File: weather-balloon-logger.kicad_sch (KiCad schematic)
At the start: 23 parts, among them J1 Conn_01x02, J2 Conn_01x11, J3 SMA, J4 SMA, J5 Conn_01x02, J6 VHF, J7 HF, Q1 IRLZ44NPBF, SW1 SPDT, U1 PCF8574N, U2 TC4422AVPA

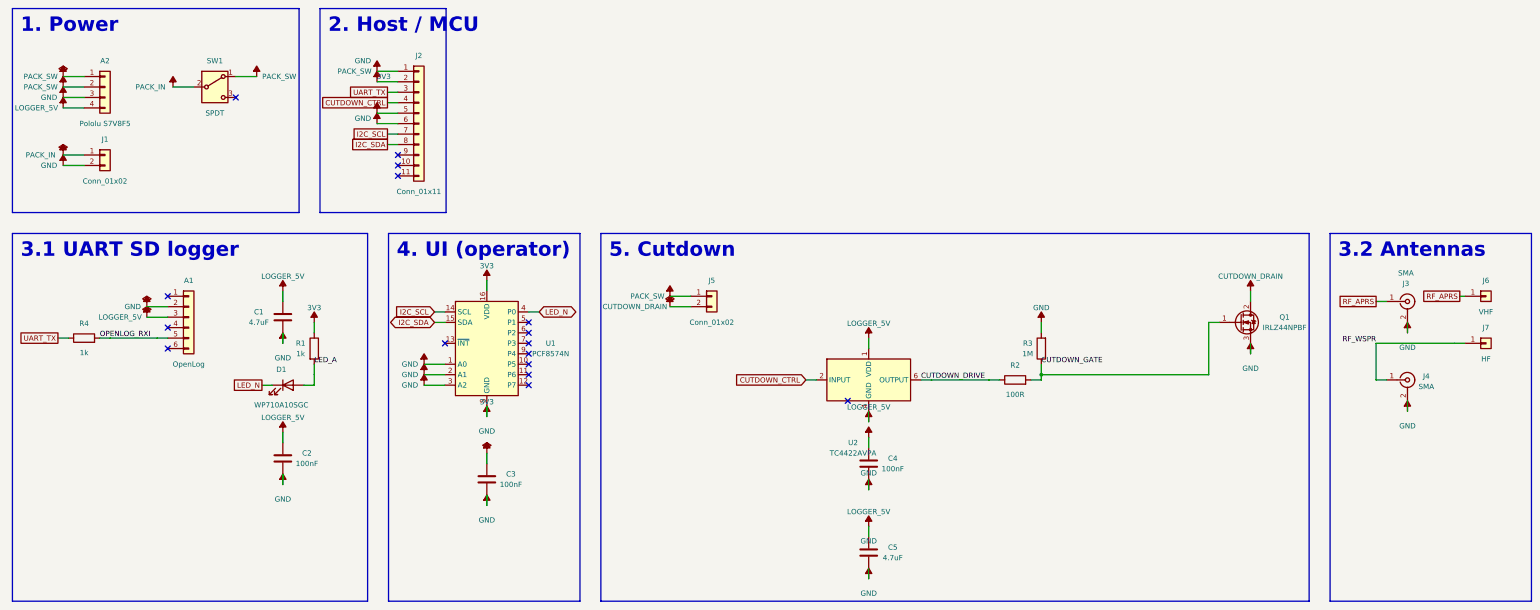
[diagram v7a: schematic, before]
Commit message: feat(schematic): migrate to LightHAB
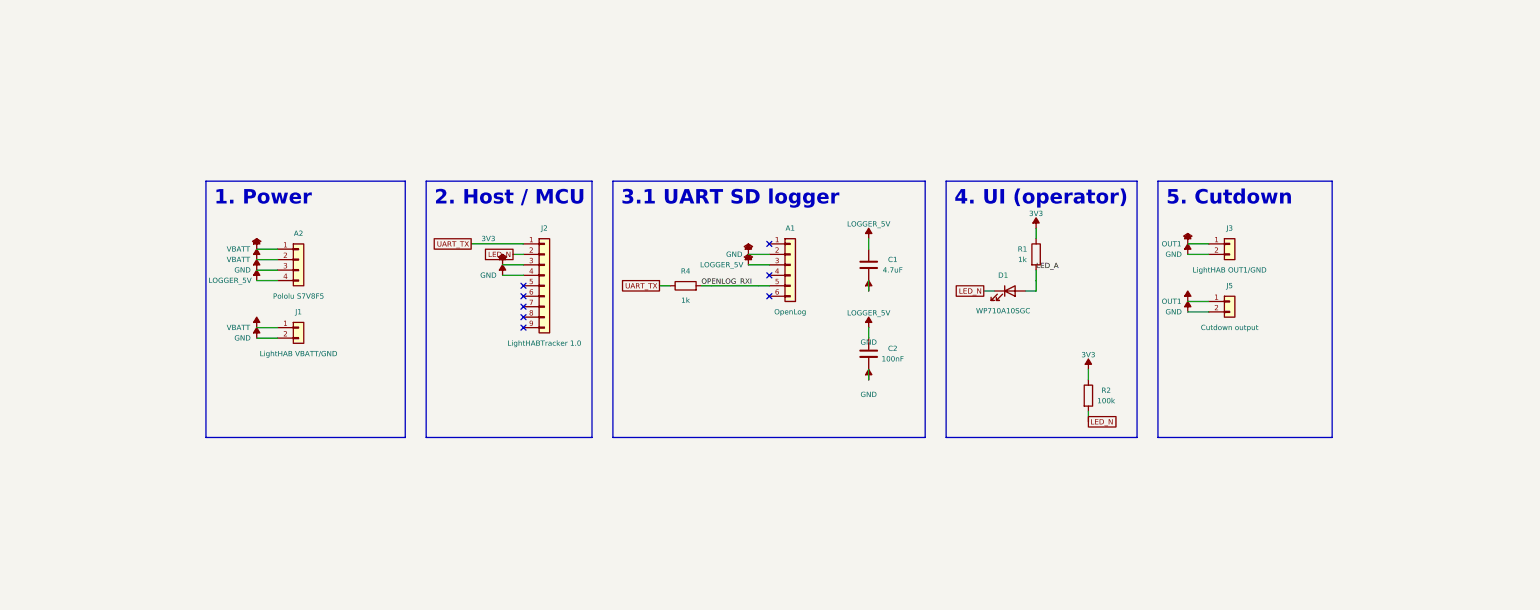
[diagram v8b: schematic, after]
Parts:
- removed C3, C4: 100nF, WeatherBalloon:KEMET_C315C104K5R5TA, symbol Device:C
- removed C5: 4.7uF, WeatherBalloon:KEMET_C322C475K5R5TA, symbol Device:C
- removed J4: SMA, Connector_Coaxial:SMA_Amphenol_132134_Vertical, symbol Connector:Conn_Coaxial
- removed J6: VHF, Connector_PinHeader_2.54mm:PinHeader_1x01_P2.54mm_Vertical, symbol Connector_Generic:Conn_01x01
- removed J7: HF, Connector_PinHeader_2.54mm:PinHeader_1x01_P2.54mm_Vertical, symbol Connector_Generic:Conn_01x01
- removed Q1: IRLZ44NPBF, Package_TO_SOT_THT:TO-220-3_Vertical, symbol Transistor_FET:IRLZ44N
- removed R3: 1M, Resistor_THT:R_Axial_DIN0207_L6.3mm_D2.5mm_P7.62mm_Horizontal, symbol Device:R
- removed SW1: SPDT, WeatherBalloon:SW_CK_7101SYZQE, symbol Switch:SW_SPDT
- removed U1: PCF8574N, Package_DIP:DIP-16_W7.62mm, symbol Interface_Expansion:PCF8574P
- removed U2: TC4422AVPA, Package_DIP:DIP-8_W7.62mm, symbol Driver_FET:TC4422
- A1: MPN DEV-13955 -> (none)
- A2: MPN Pololu item 2123 -> (none)
- C1: MPN C322C475K5R5TA -> (none)
- C2: MPN C315C104K5R5TA -> (none)
- D1: MPN WP710A10SGC -> (none)
- J1: value Conn_01x02 -> LightHAB VBATT/GND; footprint Connector_JST:JST_PH_S2B-PH-K_1x02_P2.00mm_Horizontal -> Connector_PinHeader_2.54mm:PinHeader_1x02_P2.54mm_Vertical; MPN S2B-PH-K-S(LF)(SN) -> (none)
- J2: value Conn_01x11 -> LightHABTracker 1.0; footprint Connector_PinHeader_2.54mm:PinHeader_1x11_P2.54mm_Vertical -> Connector_PinHeader_2.54mm:PinHeader_1x09_P2.54mm_Vertical; symbol Connector_Generic:Conn_01x11 -> Connector_Generic:Conn_01x09; MPN 61301111121 -> (none)
- J3: value SMA -> LightHAB OUT1/GND; footprint Connector_Coaxial:SMA_Amphenol_132134_Vertical -> Connector_PinHeader_2.54mm:PinHeader_1x02_P2.54mm_Vertical; symbol Connector:Conn_Coaxial -> Connector_Generic:Conn_01x02; MPN 132134 -> (none)
- J5: value Conn_01x02 -> Cutdown output; MPN S2B-XH-A(LF)(SN) -> (none)
- R1, R4: MPN MFR-25FBF52-1K -> (none)
- R2: value 100R -> 100k; MPN MFR-25FBF52-100R -> (none)
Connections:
- net CUTDOWN_CTRL is gone; now on net GND: J2.4 (Pin_4)
- net CUTDOWN_DRAIN is gone; now on net GND: J5.2 (Pin_2)
- net CUTDOWN_DRIVE is gone; now on net 3V3: R2.1
- net CUTDOWN_GATE is gone; now on net LED_N: R2.2
- net 3V3: now also J2.3 (Pin_3); no longer J2.5 (Pin_5)
- net GND: no longer J2.2 (Pin_2), J2.6 (Pin_6)
- net LED_N: now also J2.2 (Pin_2)
- net UART_TX: now also J2.1 (Pin_1); no longer J2.3 (Pin_3)
- net I2C_SCL: no longer names the net of J2.7 (Pin_7)
- net I2C_SDA: no longer names the net of J2.8 (Pin_8)
- net PACK_IN renamed VBATT
- net VBATT: now also A2.1 (Pin_1), A2.2 (Pin_2)
- removed net PACK_SW: A2.1 (Pin_1), A2.2 (Pin_2), J2.1 (Pin_1), J5.1 (Pin_1)
- net RF_APRS renamed OUT1
- net OUT1: now also J5.1 (Pin_1)
- no-connect marks 16 -> 8
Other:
- note removed: "3.2 Antennas"
- moved on the sheet: A1, A2, C1, C2, D1, J1, J5, R1, R2, R4
